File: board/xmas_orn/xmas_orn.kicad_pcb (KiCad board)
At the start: 2 copper layers, 27.5 x 39 mm, 17 parts, among them J1 Conn_01x07_Socket, J3 USB_C_Receptacle_USB2.0_16P, SW1 RST, SW2 BOOT, U1 ESP32-S3-MINI-1, U2 TLV75733PDBV

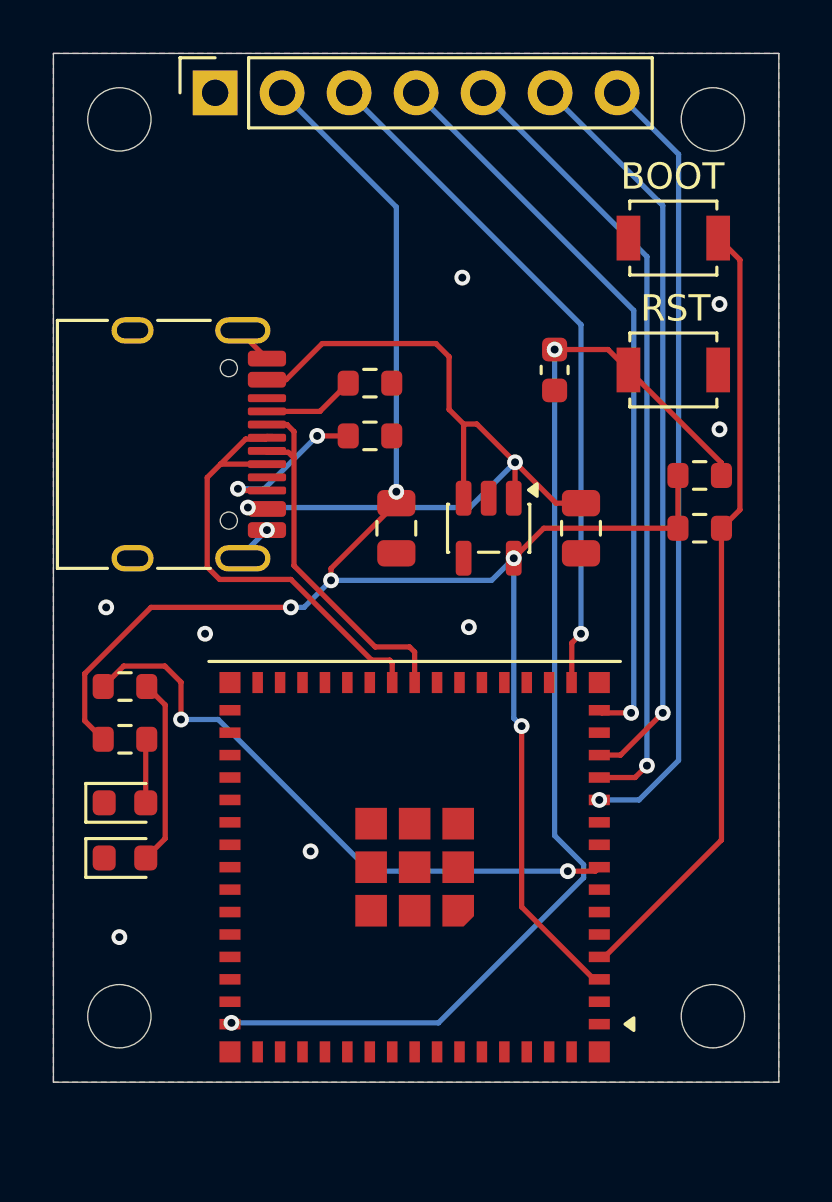
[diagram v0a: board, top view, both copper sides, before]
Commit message: Add xmas_hub 12 V -> 4 x 5 V power hub board; ornament rev 2 (WROOM-1, barrel jack)
board/xmas_hub (new KiCad 10 project): the base-of-tree distribution board for
the star topology. A 12 V barrel supply (DC-005, 5 A PTC, SMAJ15A TVS, AOD417
P-FET reverse-polarity protection, 100 uF bulk) feeds four independent
TPS54302 synchronous bucks, each with its own 2.6 A PTC, LED and 5.08 mm screw
terminal, so a fault on one arm leaves the other three running. Arms are set to
4.95 V (100k/13.7k) and feed the ornaments' DC-002 jacks over 20-22 AWG twin
lead. 80 x 66 mm, two layers, ground pours both sides.

- Schematic and PCB were bootstrapped by scripts/gen_sch.py and gen_pcb.py
  (KiCad symbol libs + bundled pcbnew); ERC and DRC with schematic parity pass.
- Every BOM line carries a verified "LCSC Part #" field; JLCPCB gerbers, drill,
  position and BOM files are in production/.
- Project footprint for the DC-005 jack: its sleeve is the lateral pin and the
  switch contact is in line with the centre pin, the opposite of KiCad's generic
  BarrelJack_Horizontal, which would have put GND on the contact that opens when
  a plug is inserted.
- docs/ has schematic/top/bottom PDFs and the datasheets the design was checked
  against; README documents the design, BOM, cable guidance and regeneration.

board/xmas_orn rev 2: ESP32-S3-WROOM-1-N16R8 module replaces the MINI-1-N8,
board grows to 27.5 x 41.5 mm, USB-C VBUS and a DNP DC-002 5 V barrel jack are
Schottky OR-ed into VIN. Project footprint/3D model for the DC-002 jack, rev 2
docs and JLCPCB outputs, and sdkconfig.rev2.defaults as an overlay for the
16 MB flash / 8 MB octal PSRAM module. Top-level README gains the rev 2 notes
and a pointer to the hub; .gitignore covers KiCad backups and lock files.

Co-Authored-By: Claude Fable 5.1 <noreply@anthropic.com>
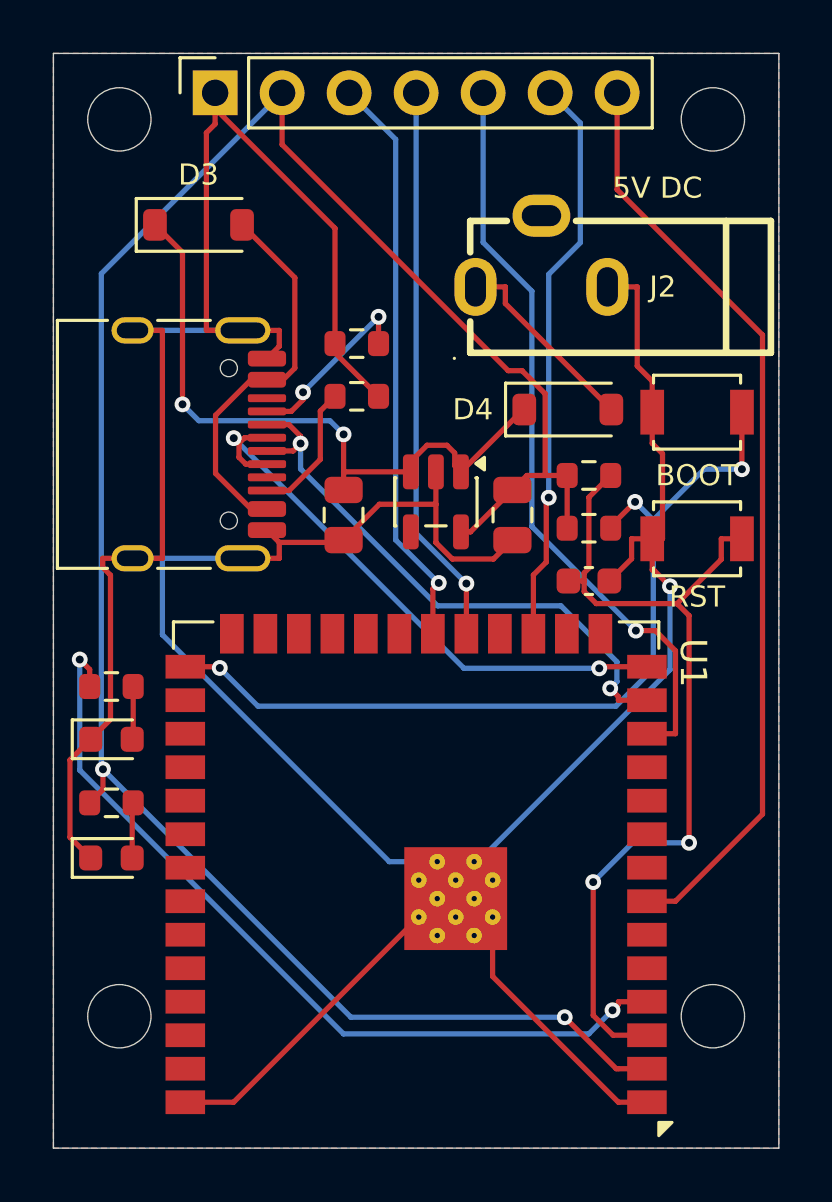
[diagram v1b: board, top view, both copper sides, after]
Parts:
- added D3: B5819W, Diode_SMD:D_SOD-123, F.Cu at (121.5, 73.5)
- added D4: B5819W, Diode_SMD:D_SOD-123, F.Cu at (135.5, 80.5)
- added J2: DC-002, xmas_orn:DC-002_BarrelJack_3.5x1.3mm_Horizontal, F.Cu at (134.5, 74.5)
- U1: value ESP32-S3-MINI-1 -> ESP32-S3-WROOM-1; footprint RF_Module:ESP32-S2-MINI-1 -> RF_Module:ESP32-S3-WROOM-1
- moved C1 9.01 mm to (127.0, 84.5)
- moved C3 8.10 mm to (136.3, 87.0), turned to 0 degrees
- moved SW2 6.66 mm to (140.4, 80.6)
- moved SW1 6.46 mm to (140.4, 85.4), turned to 0 degrees
- moved D2 4.53 mm to (118.2, 93.0)
- moved C2 4.43 mm to (133.4, 84.5)
- moved R3 4.20 mm to (136.3, 83.0)
- moved R4 4.20 mm to (136.3, 85.0)
- moved R5 2.46 mm to (118.2, 95.4)
- moved U2 2.24 mm to (130.5, 84.0)
- moved D1 2.15 mm to (118.2, 97.5)
- moved R1 1.58 mm to (127.5, 78.0), turned to 0 degrees
- moved R2 1.58 mm to (127.5, 80.0)
- moved U1 1.10 mm to (129.8, 101.5)
- moved R6 0.51 mm to (118.2, 91.0)
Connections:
- J3 pad A4: /VIN -> /VBUS
- J3 pad A9: /VIN -> /VBUS
- J3 pad B4: /VIN -> /VBUS
- J3 pad B9: /VIN -> /VBUS
- U1 pad 11: /LCD_BLK -> unconnected-(U1-IO18-Pad11)
- U1 pad 13: /LCD_DC -> /USB-
- U1 pad 14: /LCD_CS -> /USB+
- U1 pad 15: /LCD_MOSI -> unconnected-(U1-IO3-Pad15)
- U1 pad 16: /LCD_SCLK -> unconnected-(U1-IO46-Pad16)
- U1 pad 17: unconnected-(U1-IO13-Pad17) -> /LCD_DC
- U1 pad 18: unconnected-(U1-IO14-Pad18) -> /LCD_CS
- U1 pad 19: unconnected-(U1-IO15-Pad19) -> /LCD_MOSI
- U1 pad 2: GND -> /VCC
- U1 pad 20: unconnected-(U1-IO16-Pad20) -> /LCD_SCLK
- U1 pad 23: /USB- -> unconnected-(U1-IO21-Pad23)
- U1 pad 24: /USB+ -> unconnected-(U1-IO47-Pad24)
- U1 pad 27: unconnected-(U1-IO47-Pad27) -> /GPIO0
- U1 pad 3: /VCC -> /EN
- U1 pad 4: /GPIO0 -> /GPIO4
- U1 pad 40: unconnected-(U1-RXD0-Pad40) -> GND
- U1 pad 41: unconnected-(U1-IO45-Pad41) -> GND
- U1 pad 7: unconnected-(U1-IO3-Pad7) -> /LCD_BLK
- U1 pad 8: /GPIO4 -> unconnected-(U1-IO15-Pad8)
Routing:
- net GND: track 2.90 -> 154.7 mm, vias 9 -> 1
- net /VBUS: track 0.00 -> 14.7 mm
- net /VCC: track 67.8 -> 81.2 mm, vias 5 -> 2
- net /EN: track 44.8 -> 34.0 mm
- net /GPIO4: track 23.2 -> 31.6 mm
- net /VJACK: track 0.00 -> 7.45 mm
- net /USB-: track 14.5 -> 21.9 mm, vias 0 -> 2
- net /LCD_MOSI: track 28.3 -> 21.3 mm
- net /VIN: track 31.9 -> 25.1 mm
- net /LCD_DC: track 28.5 -> 21.7 mm
- net /LCD_BLK: track 30.1 -> 35.4 mm, vias 1 -> 0
- net Net-(D2-A): track 7.10 -> 2.02 mm
- net /USB+: track 17.8 -> 22.4 mm, vias 0 -> 2
- net /LCD_SCLK: track 26.3 -> 22.0 mm
- net Net-(J3-CC1): track 3.52 -> 6.89 mm, vias 0 -> 2
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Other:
- board size 27.5 x 39 mm -> 27.5 x 41.5 mm
- board text added: "5V DC"

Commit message: Gerbers: 0.05 mm solder-mask expansion on both boards
JLCPCB's minimum; at KiCad's default of 0 the mask opening equals the
pad and their DFM queried the identical USB-C shell slots on a sibling
order. pad_to_mask_clearance 0.05 in both boards, drill marks off,
gerber zips regenerated with the same file layout as before.

Co-Authored-By: Claude Fable 5.1 <noreply@anthropic.com>
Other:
- rule pad_to_mask_clearance: 0 -> 0.05
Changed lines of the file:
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@@
 	)
 	(setup
-		(pad_to_mask_clearance 0)
+		(pad_to_mask_clearance 0.05)
 		(allow_soldermask_bridges_in_footprints no)
 		(tenting
@@
 			(outputformat 1)
 			(mirror no)
-			(drillshape 1)
+			(drillshape 0)
 			(scaleselection 1)
 			(outputdirectory "")
